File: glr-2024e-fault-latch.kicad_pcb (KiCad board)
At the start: 2 copper layers, 110 x 90 mm, 70 parts, among them K101 Fujitsu_FTR-LYAA005x, K103 Fujitsu_FTR-LYAA005x, Q101 Q_NPN_BEC, Q102 Q_NPN_BEC, Q103 Q_NPN_BEC, Q104 Q_NPN_BEC, Q105 Q_NMOS_GSD, Q106 Q_NMOS_GSD, Q107 Q_PMOS_GSD, Q108 Q_PMOS_GSD, Q114 Q_NMOS_GSD, Q115 Q_NMOS_GSD, SW101 SW_Omron_B3FS, SW102 SW_Omron_B3FS, U101 SFH617A-1, U102 SFH617A-1, U104 74AHC1G00, U105 74AHC1G00, U107 74LS279, U108 641964-1, U109 SFH617A-1, U110 SFH617A-1, U112 641964-1, U115 641964-1, U116 641964-1, U120 641964-1, U123 641964-1

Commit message: add glr logo
Co-Authored-By: wallalex0 <97884125+wallalex0@users.noreply.github.com>
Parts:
- added G***: LOGO, GLR_KiCAD_Library:glr-logo, F.Cu at (129.8, 129.7)
- moved G*** 1.68 mm to (156.5, 129.6)
- moved G*** 1.68 mm to (148.3, 131.0)

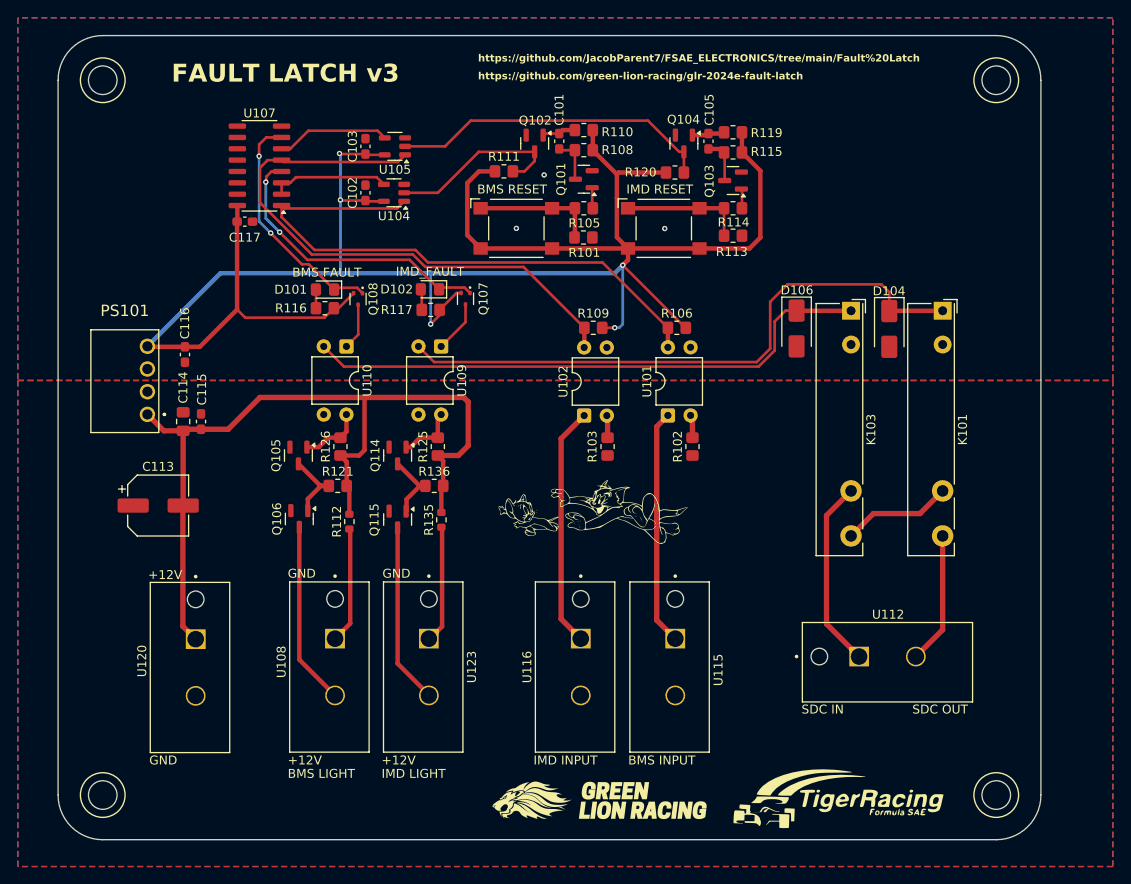
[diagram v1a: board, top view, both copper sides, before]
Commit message: use to screw terminals
improve labels in schematic

Co-Authored-By: wallalex0 <97884125+wallalex0@users.noreply.github.com>
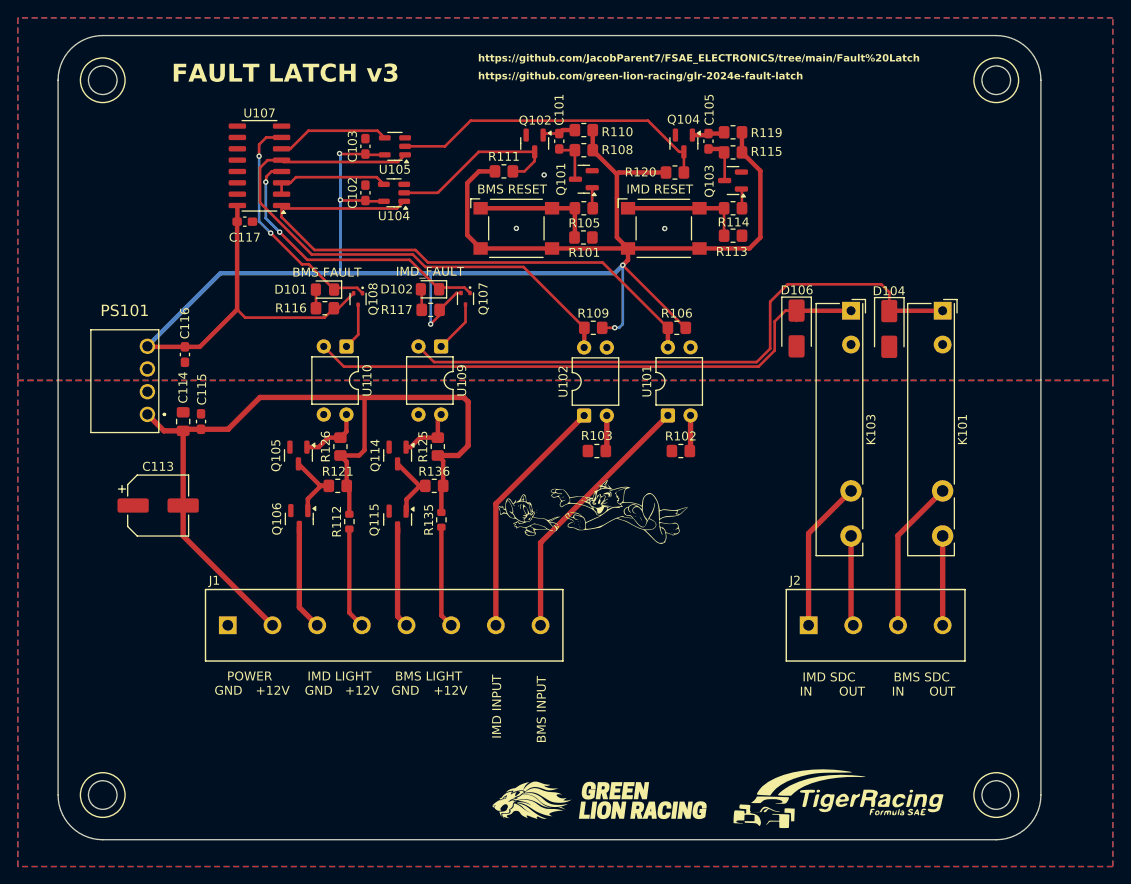
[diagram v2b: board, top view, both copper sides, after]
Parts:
- removed U108, U112, U115, U116, U120, U123: 641964-1, 641964-1:TE_641964-1
- added J1: Screw_Terminal_01x08, GLR_KiCad_Library:WECO-950-FB-08, F.Cu at (85.7, 110.5)
- added J2: Screw_Terminal_01x04, GLR_KiCad_Library:WECO-950-FB-04, F.Cu at (170.7, 109.6)
- moved R102 1.39 mm to (138.9, 90.6), turned to 0 degrees
- moved R103 1.30 mm to (129.5, 90.6), turned to 180 degrees
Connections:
- net /BMS_GREEN renamed BMS_LED
- net /BMS_SR renamed Net-(D102-K)
- net /IMD_LED renamed IMD_LED
- net /IMD_SR renamed Net-(D101-K)
- net /NBMS_LV renamed NBMS_LV
- net /NIMD_LV renamed NIMD_LV
- net /NRESET_BMS renamed BMS_NRESET
- net /NRESET_IMD renamed NRESET_IMD
- K101 pad 13: /SDC -> BMS_SDC_IN
- K101 pad 14: /SDC_OUT -> BMS_SDC_OUT
- K103 pad 13: /SDC_IN -> IMD_SDC_IN
- K103 pad 14: /SDC -> IMD_SDC_OUT
- Q106 pad 3: Net-(Q106-D) -> IMD_LED_GND
- Q115 pad 3: Net-(Q115-D) -> BMS_LED_GND
- R112 pad 2: Net-(R112-Pad2) -> IMD_LED_12V
- R135 pad 2: Net-(R135-Pad2) -> BMS_LED_12V
- U101 pad 1: /BMS_INPUT -> BMS_INPUT
- U102 pad 1: /IMD_INPUT -> IMD_INPUT
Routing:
- net BMS_INPUT: track 0.00 -> 29.4 mm
- net IMD_INPUT: track 0.00 -> 27.6 mm
- net /IMD_INPUT: track 26.9 -> 0.00 mm
- net /BMS_INPUT: track 26.4 -> 0.00 mm
- net /SDC_IN: track 21.2 -> 0.00 mm
- net Net-(Q106-D): track 20.5 -> 0.00 mm
- net Net-(Q115-D): track 20.2 -> 0.00 mm
- net BMS_SDC_IN: track 0.00 -> 17.1 mm
- net IMD_SDC_IN: track 0.00 -> 17.0 mm
- net /SDC_OUT: track 14.7 -> 0.00 mm
- net Net-(R135-Pad2): track 13.2 -> 0.00 mm
- net Net-(R112-Pad2): track 13.0 -> 0.00 mm
- net /SDC: track 12.3 -> 0.00 mm
- net IMD_LED_GND: track 0.00 -> 11.8 mm
- net BMS_LED_12V: track 0.00 -> 11.5 mm
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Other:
- board text added: "BMS SDC"
- board text added: "IMD SDC"
- board text added: "IN"
- board text added: "OUT"
- board text added: "POWER"
- board text removed: "SDC IN"
- board text removed: "SDC OUT"

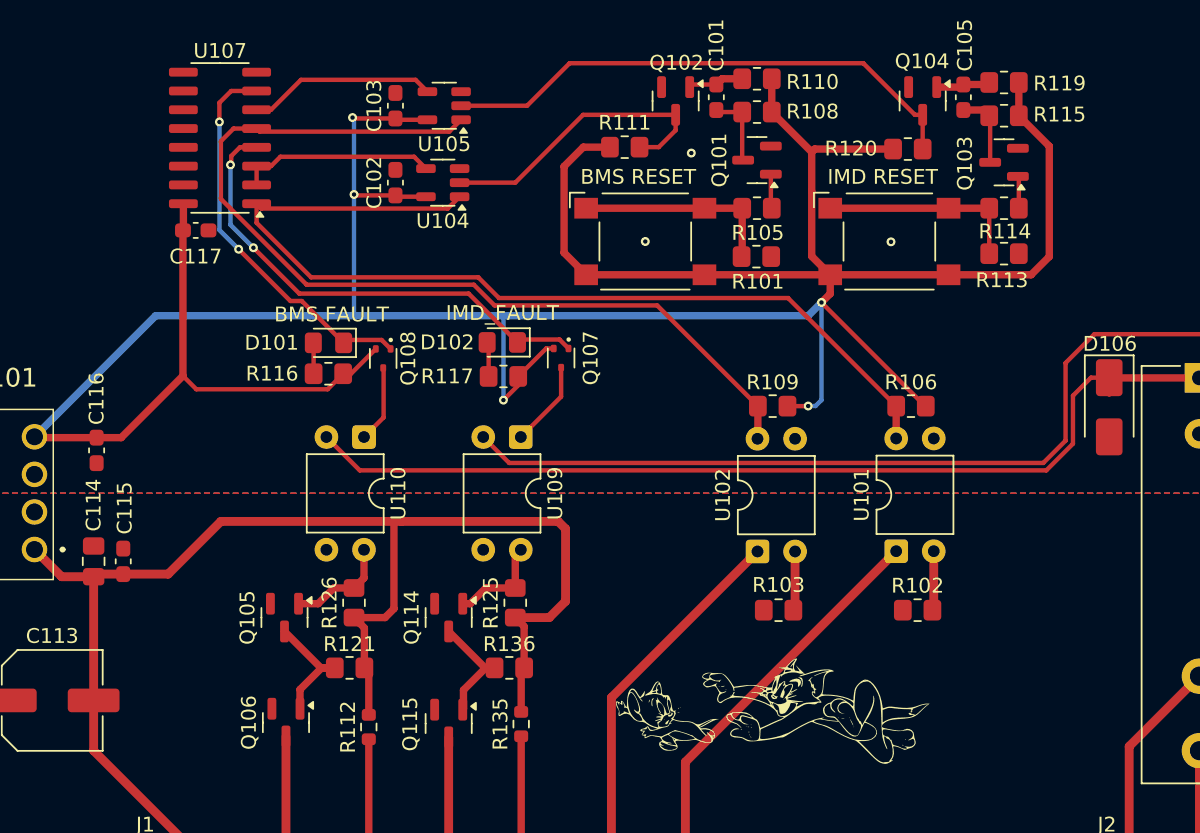
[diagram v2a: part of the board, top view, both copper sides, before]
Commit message: clean up tracks and vias
Co-Authored-By: wallalex0 <97884125+wallalex0@users.noreply.github.com>
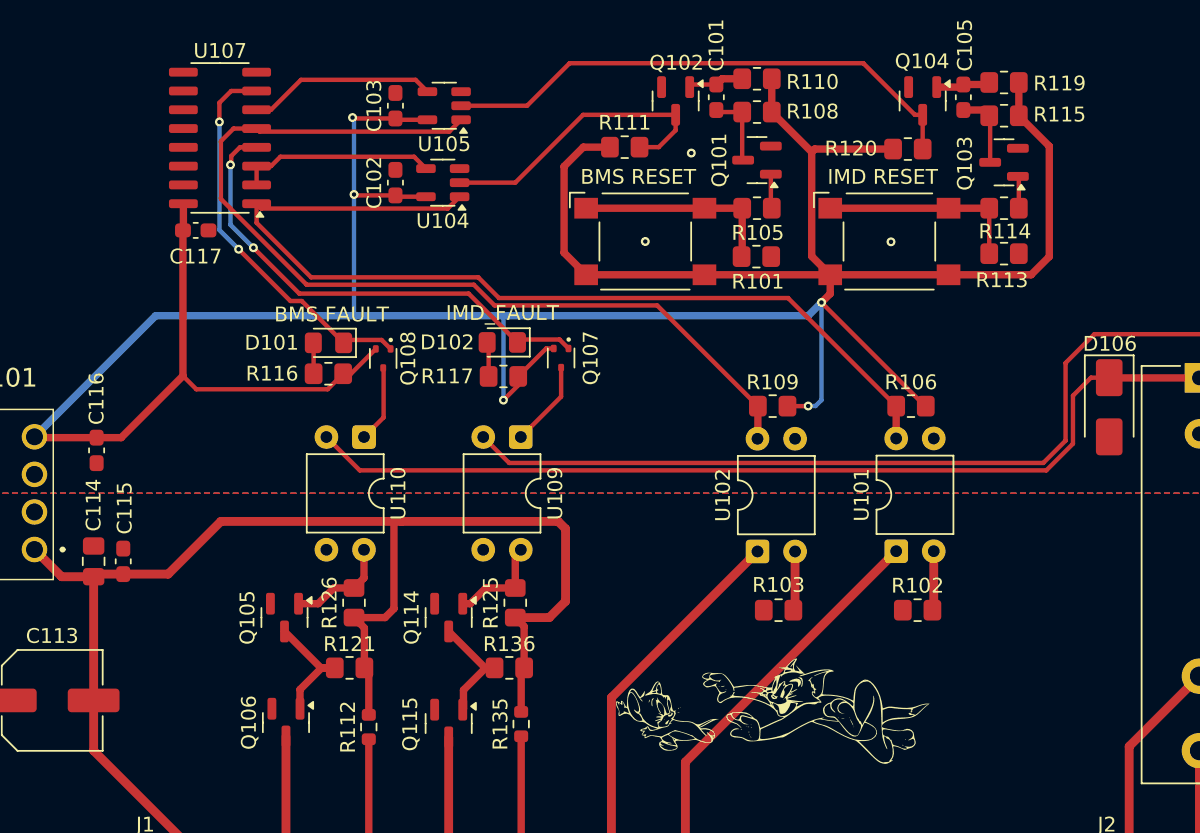
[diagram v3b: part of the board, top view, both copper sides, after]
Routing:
- net Net-(D106-K): track 65.9 -> 64.5 mm
- net unconnected-(U107C-~{R}-Pad10): track 0.63 -> 0.00 mm
